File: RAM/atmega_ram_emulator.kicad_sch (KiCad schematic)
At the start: 5 parts, among them U2 ATMEGA328-PU, Y2 16MHz

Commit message: RAM schematic complete
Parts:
- added C4: 0.1uF, Capacitor_THT:C_Disc_D5.0mm_W2.5mm_P2.50mm, symbol Device:C
- renumbered C2 to C6, C3 to C8, R2 to R11, U2 to U8
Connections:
- net +5V: now also C4.1
- net GND: now also C4.2

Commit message: Assigned footprints to all RAM components except crystal. No datasheet so waiting for delivery to hopefully get more detail or measure
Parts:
- C4: footprint Capacitor_THT:C_Disc_D5.0mm_W2.5mm_P2.50mm -> _DownloadFootprints:Cp_2mm_pin_spacing
- C6, C8: footprint (none) -> Capacitor_THT:C_Disc_D5.0mm_W2.5mm_P2.50mm
- R11: footprint (none) -> _DownloadFootprints:CF_series_Resistors_THT
- U8: footprint digikey-footprints:DIP-28_W7.62mm -> _DownloadFootprints:DIP787W46P254L3467H508Q28
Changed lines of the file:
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@@
 			)
 		)
-		(property "Footprint" "Capacitor_THT:C_Disc_D5.0mm_W2.5mm_P2.50mm"
+		(property "Footprint" "_DownloadFootprints:Cp_2mm_pin_spacing"
 			(at 39.0652 36.83 0)
 			(effects
@@
 			)
 		)
-		(property "Footprint" ""
+		(property "Footprint" "Capacitor_THT:C_Disc_D5.0mm_W2.5mm_P2.50mm"
 			(at 87.63 79.0448 0)
 			(effects
@@
 			)
 		)
-		(property "Footprint" ""
+		(property "Footprint" "Capacitor_THT:C_Disc_D5.0mm_W2.5mm_P2.50mm"
 			(at 95.25 68.8848 0)
 			(effects
@@
 			)
 		)
-		(property "Footprint" ""
+		(property "Footprint" "_DownloadFootprints:CF_series_Resistors_THT"
 			(at 46.482 33.02 90)
 			(effects
@@
 			)
 		)
-		(property "Footprint" "digikey-footprints:DIP-28_W7.62mm"
+		(property "Footprint" "_DownloadFootprints:DIP787W46P254L3467H508Q28"
 			(at 68.58 58.42 0)
 			(effects

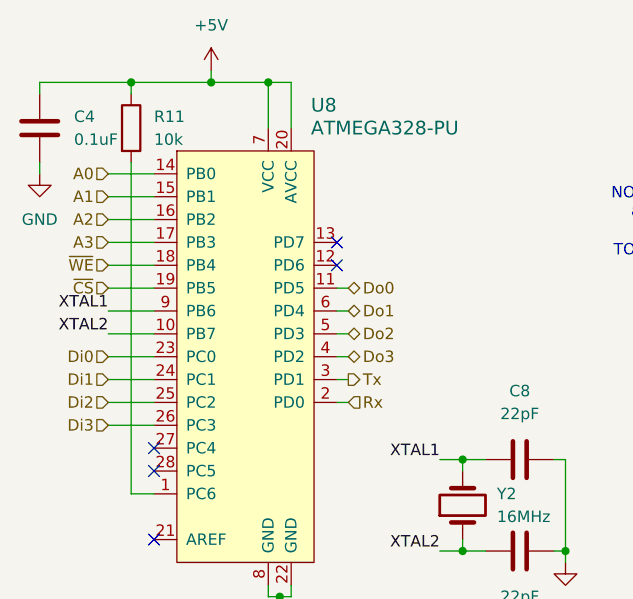
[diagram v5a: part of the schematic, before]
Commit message: RAM module layout complete except footprint for crystal
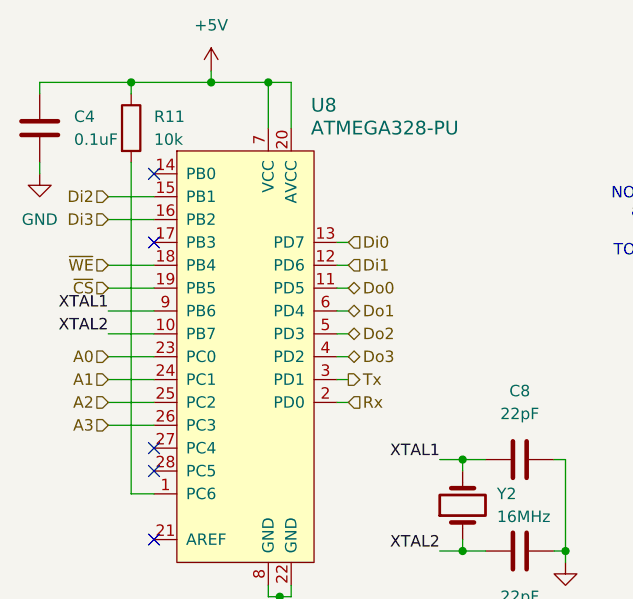
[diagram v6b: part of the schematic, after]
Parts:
- Y2: footprint (none) -> 8BitCPUFootprints:16MHzCrystalOscillator
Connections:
- net A0: now also U8.23 (PC0); no longer U8.14 (PB0)
- net A1: now also U8.24 (PC1); no longer U8.15 (PB1)
- net A2: now also U8.25 (PC2); no longer U8.16 (PB2)
- net A3: now also U8.26 (PC3); no longer U8.17 (PB3)
- net Di0: now also U8.13 (PD7); no longer U8.23 (PC0)
- net Di1: now also U8.12 (PD6); no longer U8.24 (PC1)
- net Di2: now also U8.15 (PB1); no longer U8.25 (PC2)
- net Di3: now also U8.16 (PB2); no longer U8.26 (PC3)

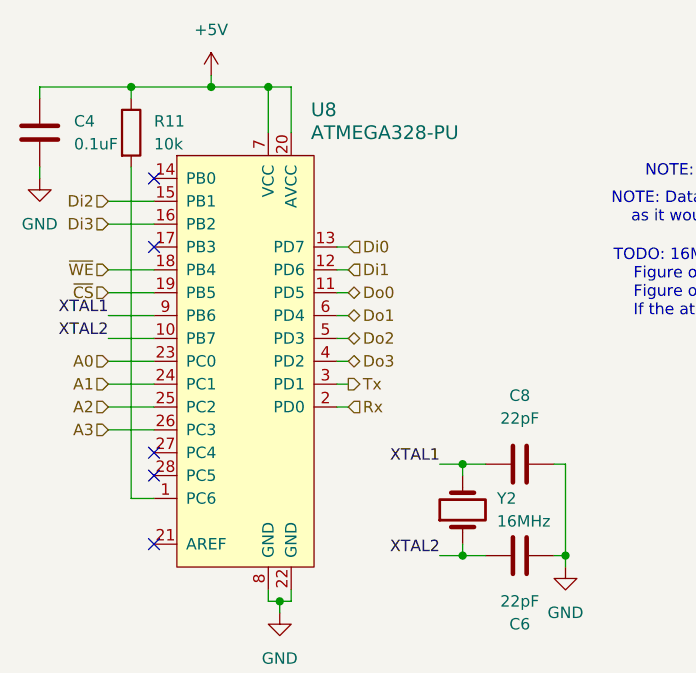
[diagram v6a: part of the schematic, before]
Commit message: Exposed SPI and RST on atmega chips
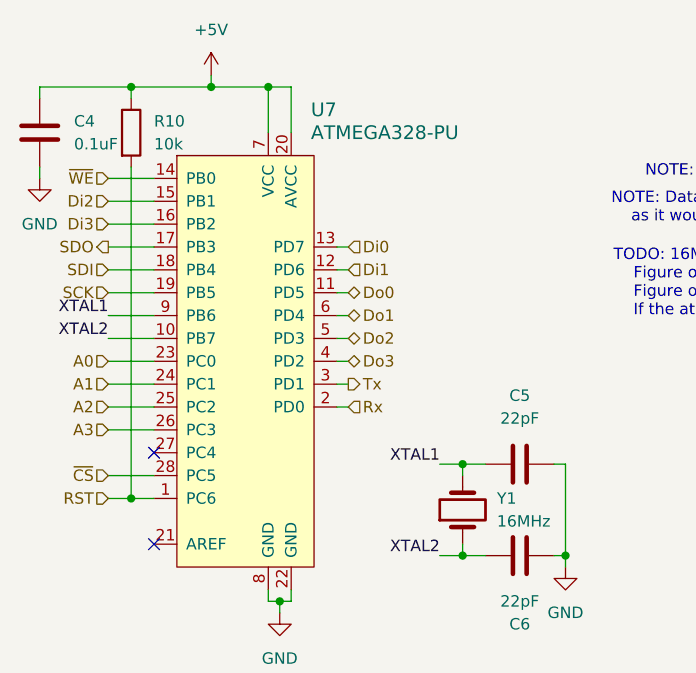
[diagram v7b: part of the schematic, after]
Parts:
- renumbered C8 to C5, R11 to R10, U8 to U7, Y2 to Y1
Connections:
- net ~{CS}: now also U7.28 (PC5); no longer U7.19 (PB5)
- net ~{WE}: now also U7.14 (PB0); no longer U7.18 (PB4)
- net RST: now reaches R10.2, U7.1 (PC6)
- net SDO: now reaches U7.17 (PB3)
- new net SCK: U7.19 (PB5)
- new net SDI: U7.18 (PB4)
- no-connect marks 5 -> 2
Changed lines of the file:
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@@
+	)
+	(junction
+		(at 48.26 73.66)
+		(diameter 0)
+		(color 0 0 0 0)
 	)
 	(junction
@@
 	)
 	(no_connect
-		(at 50.8 45.72)
-	)
-	(no_connect
-		(at 50.8 71.12)
-	)
-	(no_connect
-		(at 50.8 38.1)
-	)
-	(no_connect
 		(at 50.8 68.58)
 	)
@@
 	(wire
 		(pts
+			(xy 45.72 38.1) (xy 50.8 38.1)
+		)
+		(stroke
+			(width 0)
+			(type default)
+		)
+	)
+	(wire
+		(pts
 			(xy 96.52 80.01) (xy 96.52 69.85)
 		)
@@
 	(wire
 		(pts
+			(xy 45.72 71.12) (xy 50.8 71.12)
+		)
+		(stroke
+			(width 0)
+			(type default)
+		)
+	)
+	(wire
+		(pts
 			(xy 95.25 80.01) (xy 96.52 80.01)
 		)
@@
 		(pts
 			(xy 66.04 85.09) (xy 64.77 85.09)
+		)
+		(stroke
+			(width 0)
+			(type default)
+		)
+	)
+	(wire
+		(pts
+			(xy 45.72 73.66) (xy 48.26 73.66)
+		)
+		(stroke
+			(width 0)
+			(type default)
+		)
+	)
+	(wire
+		(pts
+			(xy 45.72 45.72) (xy 50.8 45.72)
 		)
 		(stroke
@@
 		)
 	)
+	(hierarchical_label "SCK"
+		(shape input)
+		(at 45.72 50.8 180)
+		(fields_autoplaced yes)
+		(effects
+			(font
+				(size 1.27 1.27)
+			)
+			(justify right)
+		)
+	)
 	(hierarchical_label "Rx"
 		(shape input)
@@
 		)
 	)
-	(hierarchical_label "~{WE}"
-		(shape input)
-		(at 45.72 48.26 180)
-		(fields_autoplaced yes)
-		(effects
-			(font
-				(size 1.27 1.27)
-			)
-			(justify right)
-		)
-	)
 	(hierarchical_label "Di0"
 		(shape input)
@@
 		)
 	)
+	(hierarchical_label "~{WE}"
+		(shape input)
+		(at 45.72 38.1 180)
+		(fields_autoplaced yes)
+		(effects
+			(font
+				(size 1.27 1.27)
+			)
+			(justify right)
+		)
+	)
 	(hierarchical_label "Di3"
 		(shape input)
@@
 		)
 	)
+	(hierarchical_label "~{CS}"
+		(shape input)
+		(at 45.72 71.12 180)
+		(fields_autoplaced yes)
+		(effects
+			(font
+				(size 1.27 1.27)
+			)
+			(justify right)
+		)
+	)
 	(hierarchical_label "Do1"
 		(shape bidirectional)
@@
 		)
 	)
+	(hierarchical_label "SDO"
+		(shape output)
+		(at 45.72 45.72 180)
+		(fields_autoplaced yes)
+		(effects
+			(font
+				(size 1.27 1.27)
+			)
+			(justify right)
+		)
+	)
 	(hierarchical_label "A2"
 		(shape input)
@@
 		)
 	)
-	(hierarchical_label "~{CS}"
-		(shape input)
-		(at 45.72 50.8 180)
-		(fields_autoplaced yes)
-		(effects
-			(font
-				(size 1.27 1.27)
-			)
-			(justify right)
-		)
-	)
 	(hierarchical_label "Tx"
 		(shape output)
@@
 		(shape input)
 		(at 45.72 66.04 180)
+		(fields_autoplaced yes)
+		(effects
+			(font
+				(size 1.27 1.27)
+			)
+			(justify right)
+		)
+	)
+	(hierarchical_label "RST"
+		(shape input)
+		(at 45.72 73.66 180)
+		(fields_autoplaced yes)
+		(effects
+			(font
+				(size 1.27 1.27)
+			)
+			(justify right)
+		)
+	)
+	(hierarchical_label "SDI"
+		(shape input)
+		(at 45.72 48.26 180)
 		(fields_autoplaced yes)
 		(effects
@@
 		(dnp no)
 		(fields_autoplaced yes)
-		(property "Reference" "Y2"
+		(property "Reference" "Y1"
 			(at 88.9 73.6599 90)
 			(effects
@@
 		(dnp no)
 		(fields_autoplaced yes)
-		(property "Reference" "#PWR028"
+		(property "Reference" "#PWR024"
 			(at 64.77 92.71 0)
 			(effects
@@
 		(dnp no)
 		(fields_autoplaced yes)
-		(property "Reference" "#PWR027"
+		(property "Reference" "#PWR023"
 			(at 57.15 30.48 0)
 			(effects
@@
 		(dnp no)
 		(fields_autoplaced yes)
-		(property "Reference" "C8"
+		(property "Reference" "C5"
 			(at 91.44 62.23 90)
 			(effects
@@
 		(dnp no)
 		(fields_autoplaced yes)
-		(property "Reference" "R11"
+		(property "Reference" "R10"
 			(at 50.8 31.7499 0)
 			(effects
@@
 		(dnp no)
 		(fields_autoplaced yes)
-		(property "Reference" "U8"
+		(property "Reference" "U7"
 			(at 68.2341 30.48 0)
 			(effects
@@
 		(dnp no)
 		(fields_autoplaced yes)
-		(property "Reference" "#PWR029"
+		(property "Reference" "#PWR025"
 			(at 96.52 87.63 0)
 			(effects
